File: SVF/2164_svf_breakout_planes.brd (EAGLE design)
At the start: 63.5 x 99.7 mm, 88 parts, among them IC1 SSM2164P, IC2 TL072, IC3 TL072, IC4 TL072, IC5 TL072, IC6 TL072, U1 THONKICONNNEW, U2 THONKICONNNEW, U3 THONKICONNNEW, U4 THONKICONNNEW, U5 THONKICONNNEW, U6 THONKICONNNEW

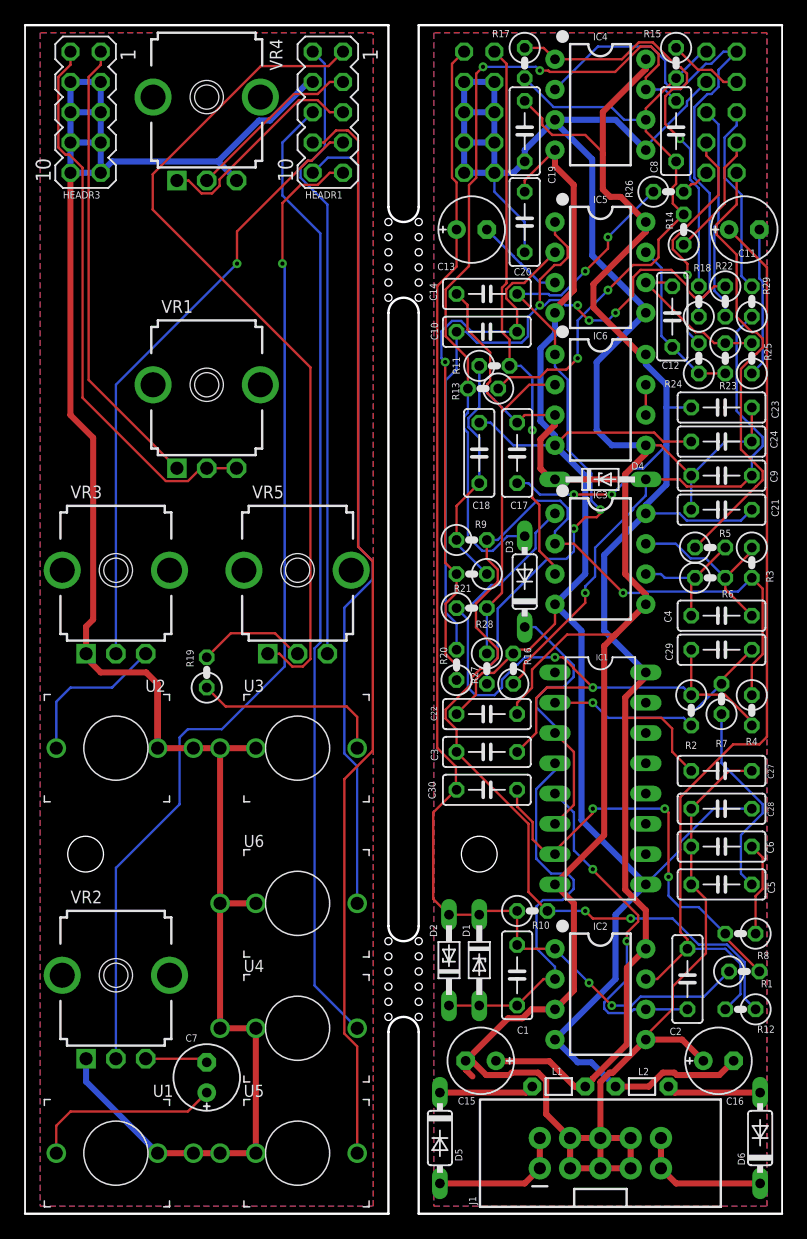
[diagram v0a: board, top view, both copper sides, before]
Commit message: Fix backwards footprint graphics for headers and power connector -- note that physical pinouts are unaffected
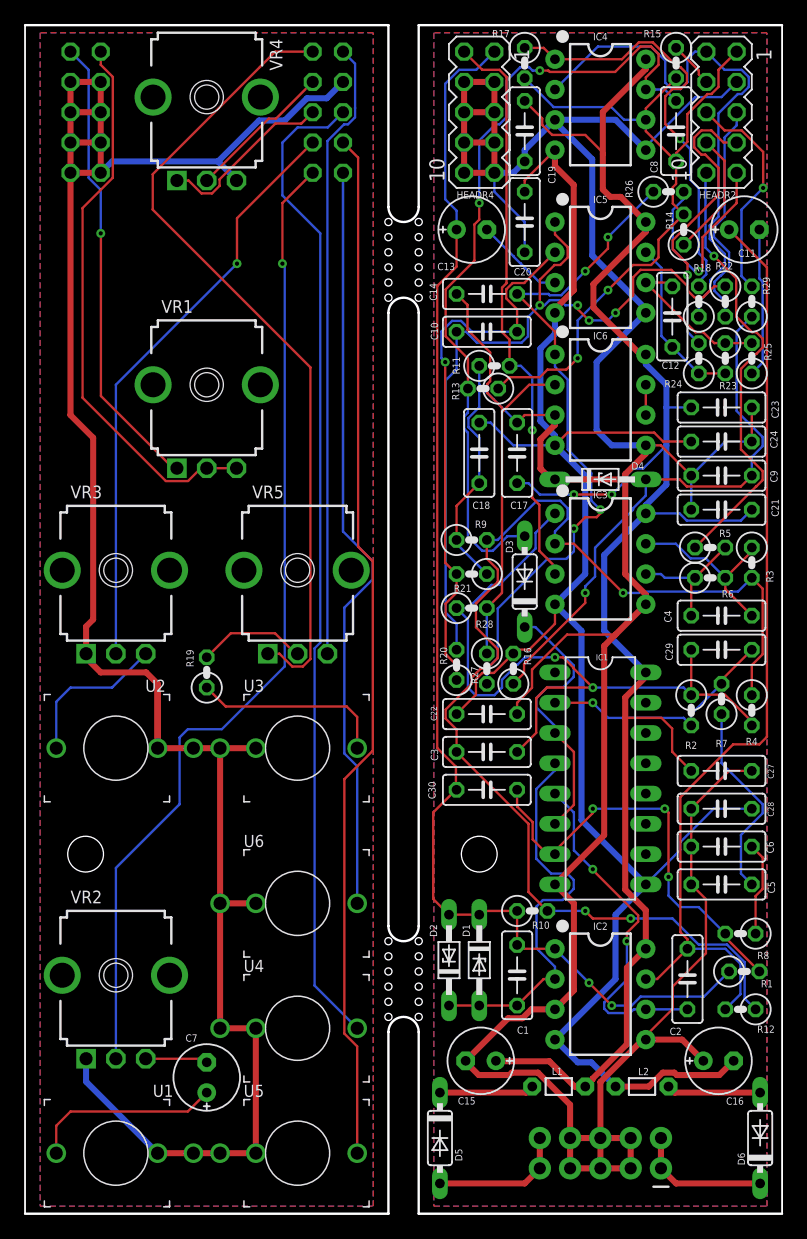
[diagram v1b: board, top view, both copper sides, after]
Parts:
- flipped HEADR1 to the top
- flipped HEADR2 to the bottom
- flipped HEADR3 to the top
- flipped HEADR4 to the bottom
- flipped J1 to the bottom
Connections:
- net N$42: now also J1.1, J1.2; no longer J1.10, J1.9
- net N$43: now also J1.10, J1.9; no longer J1.1, J1.2
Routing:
- net TO_HP_CONN: track 2.56 -> 17.7 mm, vias 0 -> 1
- net TO_CV2_POT1: track 53.4 -> 61.5 mm
- net TO_LP_CONN: track 19.8 -> 25.0 mm
- net HP_CONN: track 68.5 -> 63.7 mm
- net LP_CONN: track 91.5 -> 87.2 mm
- net AGND: track 476.1 -> 479.5 mm
- net CUTOFF_POT2: track 18.4 -> 15.0 mm
- net TO_CUTOFF_POT2: track 16.0 -> 18.5 mm, vias 0 -> 1
- net CV2_POT2: track 70.6 -> 68.1 mm
- net BP_CONN: track 80.9 -> 83.4 mm
- net CUTOFF_POT1: track 14.9 -> 12.3 mm
- net INPUT_POT: track 85.5 -> 83.0 mm
- net TO_RESO_POT1: track 105.4 -> 107.8 mm
- net TO_CUTOFF_POT1: track 6.26 -> 3.91 mm
- net TO_RESO_POT2: track 46.8 -> 48.7 mm
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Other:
- board text added: "kocmoc svf v 1.6"
- board text removed: "kocmoc svf v 1.5"

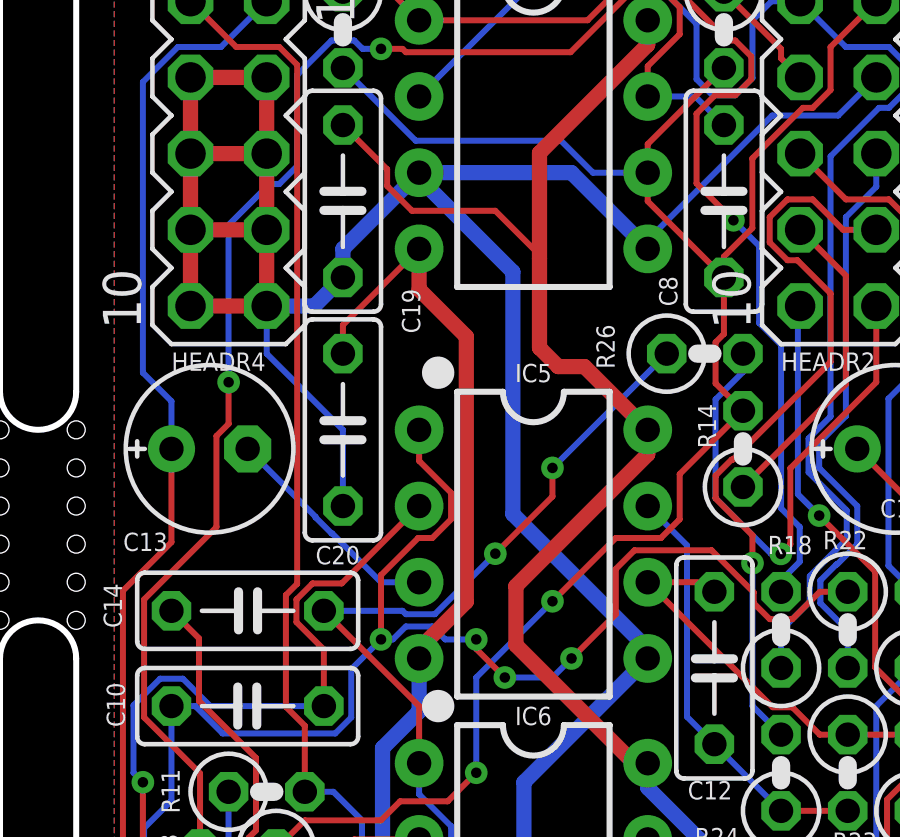
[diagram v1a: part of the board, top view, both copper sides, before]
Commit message: Fix bandpass output AC biasing issue
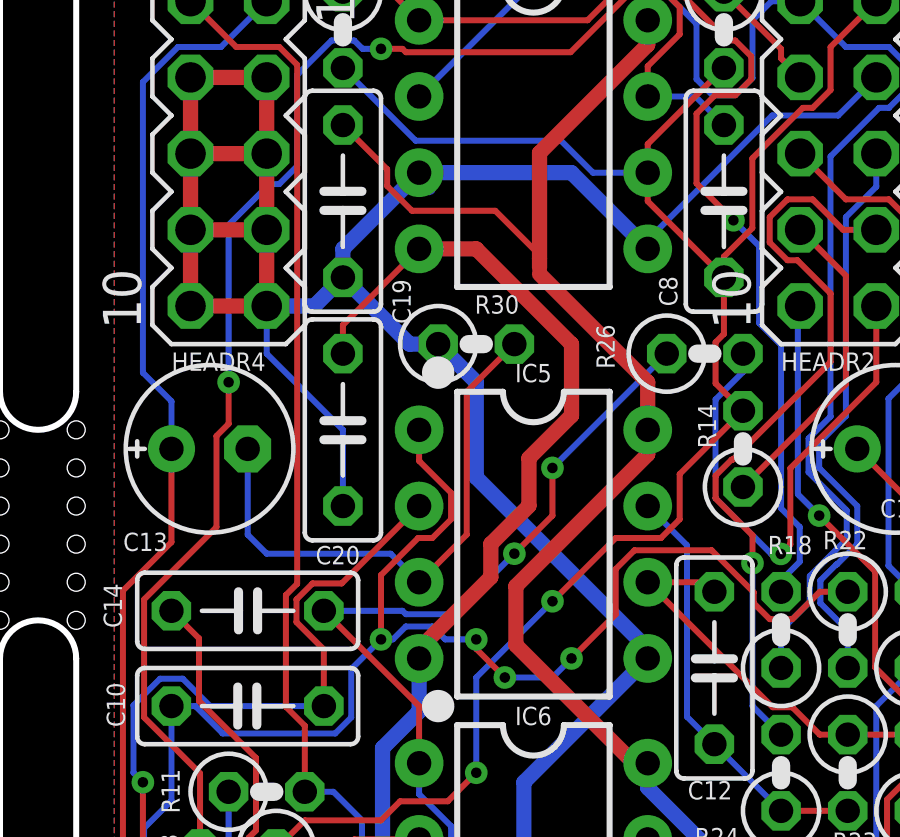
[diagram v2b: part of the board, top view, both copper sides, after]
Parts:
- added R30: 17k, rcl:0207/2V
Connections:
- removed net N$30: C13.-, IC5.3
- new net N$3: C13.-, IC5.3, R30.2
- net AGND: now also R30.1
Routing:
- net N$3: track 0.00 -> 18.5 mm
- net N$30: track 7.57 -> 0.00 mm
- net V-: track 152.6 -> 156.6 mm
- net AGND: track 479.5 -> 478.3 mm
- net V+: track 153.6 -> 153.1 mm
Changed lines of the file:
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@@
 </element>
 <element name="C19" library="rcl" library_urn="urn:adsk.eagle:library:334" package="C050-025X075" package3d_urn="urn:adsk.eagle:package:23637/1" value="100n" x="41.91" y="90.805" smashed="yes" rot="R90">
-<attribute name="NAME" x="43.8785" y="87.884" size="0.6096" layer="25" ratio="10" rot="R270"/>
+<attribute name="NAME" x="43.561" y="88.2015" size="0.6096" layer="25" ratio="10" rot="R270"/>
 <attribute name="POPULARITY" value="29" x="41.91" y="90.805" size="1.778" layer="27" font="vector" rot="R90" display="off"/>
 <attribute name="SPICEPREFIX" value="C" x="41.91" y="90.805" size="1.778" layer="27" font="vector" rot="R90" display="off"/>
@@
 </element>
 <element name="U$1" library="oshw" package="OSHW_5MM" value="" x="48.26" y="89.8525" smashed="yes" rot="SMR270"/>
+<element name="R30" library="rcl" library_urn="urn:adsk.eagle:library:334" package="0207/2V" package3d_urn="urn:adsk.eagle:package:23490/1" value="17k" x="46.355" y="86.0425" smashed="yes">
+<attribute name="NAME" x="46.3042" y="87.0585" size="0.6096" layer="25" ratio="10"/>
+<attribute name="POPULARITY" value="17" x="46.355" y="86.0425" size="1.778" layer="27" display="off"/>
+<attribute name="SPICEPREFIX" value="R" x="46.355" y="86.0425" size="1.778" layer="27" display="off"/>
+<attribute name="VALUE" x="46.3042" y="83.8073" size="1.27" layer="27" ratio="10"/>
+</element>
 </elements>
 <signals>
@@
 <wire x1="41.91" y1="88.265" x2="40.9575" y2="87.3125" width="0.508" layer="16"/>
 <wire x1="44.7675" y1="91.2592125" x2="44.7675" y2="91.7575" width="0.508" layer="16"/>
-<wire x1="47.5742" y1="88.4525125" x2="44.7675" y2="91.2592125" width="0.508" layer="16"/>
-<wire x1="47.5742" y1="80.3783" x2="47.5742" y2="88.4525125" width="0.508" layer="16"/>
 <wire x1="52.07" y1="75.565" x2="52.07" y2="75.8825" width="0.508" layer="16"/>
-<wire x1="52.07" y1="75.8825" x2="47.5742" y2="80.3783" width="0.508" layer="16"/>
 <wire x1="44.45" y1="61.595" x2="44.1325" y2="61.595" width="0.2" layer="1"/>
 <wire x1="55.88" y1="33.9725" x2="55.88" y2="30.7975" width="0.2" layer="1"/>
@@
 <vertex x="1.27" y="99.06"/>
 </polygon>
-<wire x1="36.83" y1="94.9325" x2="26.67" y2="94.9325" width="0" layer="19" extent="1-1"/>
+<contactref element="R30" pad="1"/>
+<wire x1="46.355" y1="84.7725" x2="45.085" y2="86.0425" width="0.508" layer="16"/>
+<wire x1="52.07" y1="75.8825" x2="46.355" y2="81.5975" width="0.508" layer="16"/>
+<wire x1="46.355" y1="81.5975" x2="46.355" y2="84.7725" width="0.508" layer="16"/>
+<wire x1="45.085" y1="86.0425" x2="44.1325" y2="86.0425" width="0.508" layer="16"/>
+<wire x1="44.1325" y1="86.0425" x2="41.91" y2="88.265" width="0.508" layer="16"/>
+<wire x1="26.67" y1="94.9325" x2="36.83" y2="94.9325" width="0" layer="19" extent="1-1"/>
 </signal>
 <signal name="N$2">
@@
 <wire x1="46.355" y1="12.7" x2="44.45" y2="14.605" width="0.508" layer="16"/>
 <wire x1="44.45" y1="75.565" x2="44.45" y2="75.8824125" width="0.508" layer="1"/>
-<wire x1="44.45" y1="87.8686875" x2="44.45" y2="89.2175" width="0.508" layer="1"/>
-<wire x1="44.45" y1="75.8824125" x2="46.0216" y2="77.4540125" width="0.508" layer="1"/>
-<wire x1="46.0216" y1="86.2970875" x2="44.45" y2="87.8686875" width="0.508" layer="1"/>
-<wire x1="46.0216" y1="77.4540125" x2="46.0216" y2="86.2970875" width="0.508" layer="1"/>
 <wire x1="52.07" y1="27.6225" x2="54.9672" y2="30.5197" width="0.2" layer="16"/>
 <wire x1="54.9672" y1="30.5197" x2="54.9672" y2="31.1756" width="0.2" layer="16"/>
@@
 <wire x1="40.9575" y1="64.4525" x2="39.0525" y2="66.3575" width="0.2" layer="16"/>
 <wire x1="39.0525" y1="66.3575" x2="38.1" y2="66.3575" width="0.2" layer="16"/>
+<wire x1="46.8404" y1="78.2728125" x2="46.8404" y2="79.38249375" width="0.508" layer="1"/>
+<wire x1="44.45" y1="75.8824125" x2="46.8404" y2="78.2728125" width="0.508" layer="1"/>
+<wire x1="48.1104" y1="80.65249375" x2="48.1104" y2="82.23999375" width="0.508" layer="1"/>
+<wire x1="48.1104" y1="82.23999375" x2="49.53" y2="83.65959375" width="0.508" layer="1"/>
+<wire x1="49.53" y1="86.0425" x2="46.355" y2="89.2175" width="0.508" layer="1"/>
+<wire x1="46.8404" y1="79.38249375" x2="48.1104" y2="80.65249375" width="0.508" layer="1"/>
+<wire x1="49.53" y1="83.65959375" x2="49.53" y2="86.0425" width="0.508" layer="1"/>
+<wire x1="46.355" y1="89.2175" x2="44.45" y2="89.2175" width="0.508" layer="1"/>
 </signal>
 <signal name="N$23">
@@
 <wire x1="51.628775" y1="79.1702" x2="54.2007" y2="79.1702" width="0.2" layer="1"/>
 </signal>
-<signal name="N$30">
-<contactref element="IC5" pad="3"/>
-<contactref element="C13" pad="-"/>
-<wire x1="38.735" y1="82.55" x2="40.9972" y2="80.2878" width="0.2" layer="16"/>
-<wire x1="40.9972" y1="80.2878" x2="40.9972" y2="80.2669" width="0.2" layer="16"/>
-<wire x1="40.9972" y1="80.2669" x2="41.5319" y2="79.7322" width="0.2" layer="16"/>
-<wire x1="41.5319" y1="79.7322" x2="41.5528" y2="79.7322" width="0.2" layer="16"/>
-<wire x1="41.5528" y1="79.7322" x2="43.18" y2="78.105" width="0.2" layer="16"/>
-<wire x1="43.18" y1="78.105" x2="44.45" y2="78.105" width="0.2" layer="16"/>
-</signal>
 <signal name="N$31">
 <contactref element="IC5" pad="6"/>
@@
 <wire x1="52.705" y1="85.725" x2="48.895" y2="81.915" width="0.2" layer="16"/>
 <via x="48.895" y="81.915" extent="1-16" drill="0.35"/>
-<wire x1="48.895" y1="81.915" x2="48.895" y2="80.9625" width="0.2" layer="1"/>
-<wire x1="48.895" y1="80.9625" x2="46.99" y2="79.0575" width="0.2" layer="1"/>
-<via x="46.99" y="79.0575" extent="1-16" drill="0.35"/>
+<wire x1="48.895" y1="81.915" x2="48.895" y2="80.3275" width="0.2" layer="1"/>
+<wire x1="48.895" y1="80.3275" x2="47.625" y2="79.0575" width="0.2" layer="1"/>
+<via x="47.625" y="79.0575" extent="1-16" drill="0.35"/>
 <wire x1="44.008775" y1="77.0398" x2="43.896075" y2="77.1525" width="0.2" layer="16"/>
 <wire x1="43.896075" y1="77.1525" x2="41.275" y2="77.1525" width="0.2" layer="16"/>
-<wire x1="46.99" y1="79.0575" x2="44.9723" y2="77.0398" width="0.2" layer="16"/>
-<wire x1="44.9723" y1="77.0398" x2="44.008775" y2="77.0398" width="0.2" layer="16"/>
+<wire x1="47.625" y1="79.0575" x2="45.6073" y2="77.0398" width="0.2" layer="16"/>
+<wire x1="45.6073" y1="77.0398" x2="44.008775" y2="77.0398" width="0.2" layer="16"/>
 <wire x1="39.6478" y1="50.7603" x2="43.815" y2="54.9275" width="0.2" layer="16"/>
 <wire x1="38.735" y1="44.45" x2="38.735" y2="45.6991" width="0.2" layer="16"/>
@@
 <wire x1="50.4825" y1="20.6375" x2="52.07" y2="22.225" width="0.508" layer="1"/>
 <wire x1="50.4825" y1="14.20681875" x2="50.4825" y2="20.6375" width="0.508" layer="1"/>
-<wire x1="52.07" y1="83.185" x2="49.9618" y2="85.2932" width="0.508" layer="1"/>
-<wire x1="49.9618" y1="85.2932" x2="49.0881125" y2="85.2932" width="0.508" layer="1"/>
-<wire x1="49.0881125" y1="85.2932" x2="48.4632" y2="85.9181125" width="0.508" layer="1"/>
-<wire x1="48.4632" y1="85.9181125" x2="48.4632" y2="88.9" width="0.508" layer="1"/>
+<wire x1="52.07" y1="83.185" x2="52.07" y2="84.7725" width="0.508" layer="1"/>
+<wire x1="52.07" y1="84.7725" x2="48.4632" y2="88.3793" width="0.508" layer="1"/>
 <wire x1="48.4632" y1="88.9" x2="48.4632" y2="92.4149125" width="0.508" layer="1"/>
 <wire x1="48.4632" y1="92.4149125" x2="52.07" y2="96.0217125" width="0.508" layer="1"/>
@@
 <wire x1="46.99" y1="90.4875" x2="48.4632" y2="89.0143" width="0.2" layer="1"/>
 <wire x1="48.4632" y1="89.0143" x2="48.4632" y2="88.9" width="0.2" layer="1"/>
+<wire x1="48.4632" y1="88.3793" x2="48.4632" y2="88.5825" width="0.2" layer="1"/>
 <wire x1="52.07" y1="45.4025" x2="48.5775" y2="48.895" width="0.508" layer="16"/>
 <wire x1="48.5775" y1="48.895" x2="48.5775" y2="55.245" width="0.508" layer="16"/>
@@
 <wire x1="49.2125" y1="60.325" x2="50.4968" y2="61.6093" width="0.2" layer="16"/>
 <wire x1="50.4968" y1="61.6093" x2="50.4968" y2="61.9731" width="0.2" layer="16"/>
+<wire x1="48.4632" y1="88.5825" x2="48.4632" y2="88.9" width="0.508" layer="1"/>
 </signal>
 <signal name="TO_CV2_POT1">
@@
 <wire x1="41.8545" y1="46.10218125" x2="46.99" y2="51.23768125" width="0.2" layer="1"/>
 </signal>
+<signal name="N$3">
+<contactref element="C13" pad="-"/>
+<contactref element="R30" pad="2"/>
+<contactref element="IC5" pad="3"/>
+<wire x1="44.45" y1="78.105" x2="46.0375" y2="79.6925" width="0.2" layer="1"/>
+<wire x1="38.735" y1="82.55" x2="38.735" y2="79.6925" width="0.2" layer="16"/>
+<wire x1="38.735" y1="79.6925" x2="39.37" y2="79.0575" width="0.2" layer="16"/>
+<wire x1="39.37" y1="79.0575" x2="43.4975" y2="79.0575" width="0.2" layer="16"/>
+<wire x1="43.4975" y1="79.0575" x2="44.45" y2="78.105" width="0.2" layer="16"/>
+<wire x1="46.0375" y1="84.455" x2="47.625" y2="86.0425" width="0.2" layer="1"/>
+<wire x1="46.0375" y1="79.6925" x2="46.0375" y2="84.455" width="0.2" layer="1"/>
+</signal>
 </signals>

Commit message: Trim output gains for more conservative levels
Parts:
- R20: value 77k -> 68k
- R23, R27: value 100k -> 33k
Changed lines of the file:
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@@
 <drawing>
 <settings>
-<setting alwaysvectorfont="yes"/>
+<setting alwaysvectorfont="no"/>
 <setting verticaltext="up"/>
 </settings>
@@
 </layers>
 <board>
-<fusionsync huburn="a.YnVzaW5lc3M6cmFkaW9mcmVlcm9ib3Ryb24" projecturn="a.YnVzaW5lc3M6cmFkaW9mcmVlcm9ib3Ryb24jRDIwMjAwNjIyMzEwMDUxMTMx" f3durn="urn:adsk.wipprod:dm.lineage:cmH7f9pKSfelTlhE1K4e4Q" pcbguid="" lastpulledtime="" lastsyncedchangeguid="" latestrevisionid="fc74734c-3a24-43ac-8080-12a2ecc2c1ff" lastsyncedrevisionid="fc74734c-3a24-43ac-8080-12a2ecc2c1ff" lastboardhashguid="a217513c-74f0-9a54-c2f0-9dbf27f5bf64" lastpushedtime="2021-04-19T12:52:39Z" linktopcb3d="true"/>
+<fusionsync huburn="a.YnVzaW5lc3M6cmFkaW9mcmVlcm9ib3Ryb24" projecturn="a.YnVzaW5lc3M6cmFkaW9mcmVlcm9ib3Ryb24jRDIwMjAwNjIyMzEwMDUxMTMx" f3durn="urn:adsk.wipprod:dm.lineage:cmH7f9pKSfelTlhE1K4e4Q" pcbguid="" lastpulledtime="" lastsyncedchangeguid="" latestrevisionid="fc74734c-3a24-43ac-8080-12a2ecc2c1ff" lastsyncedrevisionid="fc74734c-3a24-43ac-8080-12a2ecc2c1ff" lastboardhashguid="a217513c-74f0-9a54-c2f0-9dbf27f5bf64" lastpushedtime="2021-04-19T12:52:39Z" linktopcb3d="false"/>
 <plain>
 <wire x1="0" y1="0" x2="0" y2="99.695" width="0.1524" layer="20"/>
@@
 <attribute name="VALUE" x="56.1594" y="39.0525" size="0.6096" layer="27" ratio="10"/>
 </element>
-<element name="R20" library="rcl" library_urn="urn:adsk.eagle:library:334" package="0207/2V" package3d_urn="urn:adsk.eagle:package:23490/1" value="77k" x="36.195" y="46.0375" smashed="yes" rot="R90">
+<element name="R20" library="rcl" library_urn="urn:adsk.eagle:library:334" package="0207/2V" package3d_urn="urn:adsk.eagle:package:23490/1" value="68k" x="36.195" y="46.0375" smashed="yes" rot="R90">
 <attribute name="NAME" x="35.41201875" y="46.058709375" size="0.6096" layer="25" ratio="10" rot="R90"/>
 <attribute name="POPULARITY" value="17" x="136.525" y="128.5875" size="1.778" layer="27" rot="R90" display="off"/>
@@
 <attribute name="VALUE" x="57.4675" y="76.2381" size="0.6096" layer="27" ratio="10" rot="R270"/>
 </element>
-<element name="R23" library="rcl" library_urn="urn:adsk.eagle:library:334" package="0207/2V" package3d_urn="urn:adsk.eagle:package:23490/1" value="100k" x="58.7375" y="71.755" smashed="yes" rot="R270">
+<element name="R23" library="rcl" library_urn="urn:adsk.eagle:library:334" package="0207/2V" package3d_urn="urn:adsk.eagle:package:23490/1" value="33k" x="58.7375" y="71.755" smashed="yes" rot="R270">
 <attribute name="NAME" x="58.2295" y="69.1515" size="0.6096" layer="25" ratio="10"/>
 <attribute name="POPULARITY" value="17" x="-46.6725" y="27.305" size="1.778" layer="27" rot="R270" display="off"/>
@@
 <attribute name="VALUE" x="51.0794" y="84.455" size="0.6096" layer="27" ratio="10"/>
 </element>
-<element name="R27" library="rcl" library_urn="urn:adsk.eagle:library:334" package="0207/2V" package3d_urn="urn:adsk.eagle:package:23490/1" value="100k" x="38.735" y="45.72" smashed="yes" rot="R270">
+<element name="R27" library="rcl" library_urn="urn:adsk.eagle:library:334" package="0207/2V" package3d_urn="urn:adsk.eagle:package:23490/1" value="33k" x="38.735" y="45.72" smashed="yes" rot="R270">
 <attribute name="NAME" x="37.4015" y="45.9105" size="0.6096" layer="25" ratio="10" rot="R270"/>
 <attribute name="POPULARITY" value="17" x="-71.755" y="26.67" size="1.778" layer="27" rot="R270" display="off"/>

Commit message: Add V1.7 files for SVF
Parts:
- added D7: BAT85, diode:DO35-7
- moved C2 1.27 mm to (54.3, 19.7)
- moved R8 1.00 mm to (60.3, 22.5)
- moved D1 0.95 mm to (39.1, 21.3)
- moved D2 0.95 mm to (36.5, 21.3)
- moved C1 0.63 mm to (41.9, 20.0)
- moved R10 0.63 mm to (43.2, 25.4)
- moved R20 0.32 mm to (36.2, 45.7)
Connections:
- net AGND: now also D7.C
- net V-: now also D7.A
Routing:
- net V+: track 153.1 -> 159.3 mm
- net AGND: track 478.3 -> 482.6 mm
- net V-: track 156.6 -> 159.8 mm
- net N$16: track 7.93 -> 9.03 mm
- net N$1: track 33.6 -> 32.6 mm
- net N$9: track 102.5 -> 103.2 mm
- net N$2: track 29.4 -> 30.0 mm
- net TO_RESO_POT1: track 107.8 -> 107.3 mm
- net N$4: track 36.1 -> 35.6 mm
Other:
- outline, holes or cut-outs redrawn
- board text added: "kocmoc svf v 1.7"
- board text removed: "kocmoc svf v 1.6"
